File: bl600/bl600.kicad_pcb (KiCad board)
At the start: 2 copper layers, 50 x 50 mm, 27 parts, among them IC1 BL600, IC2 LK112, P1 CONN_4, P2 CONN_3X2, P4 CONN_2, P5 CONN_8, P6 CONN_8, P7 CONN_6X2, Q1 MOSFET_P, Q2 MOSFET_P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

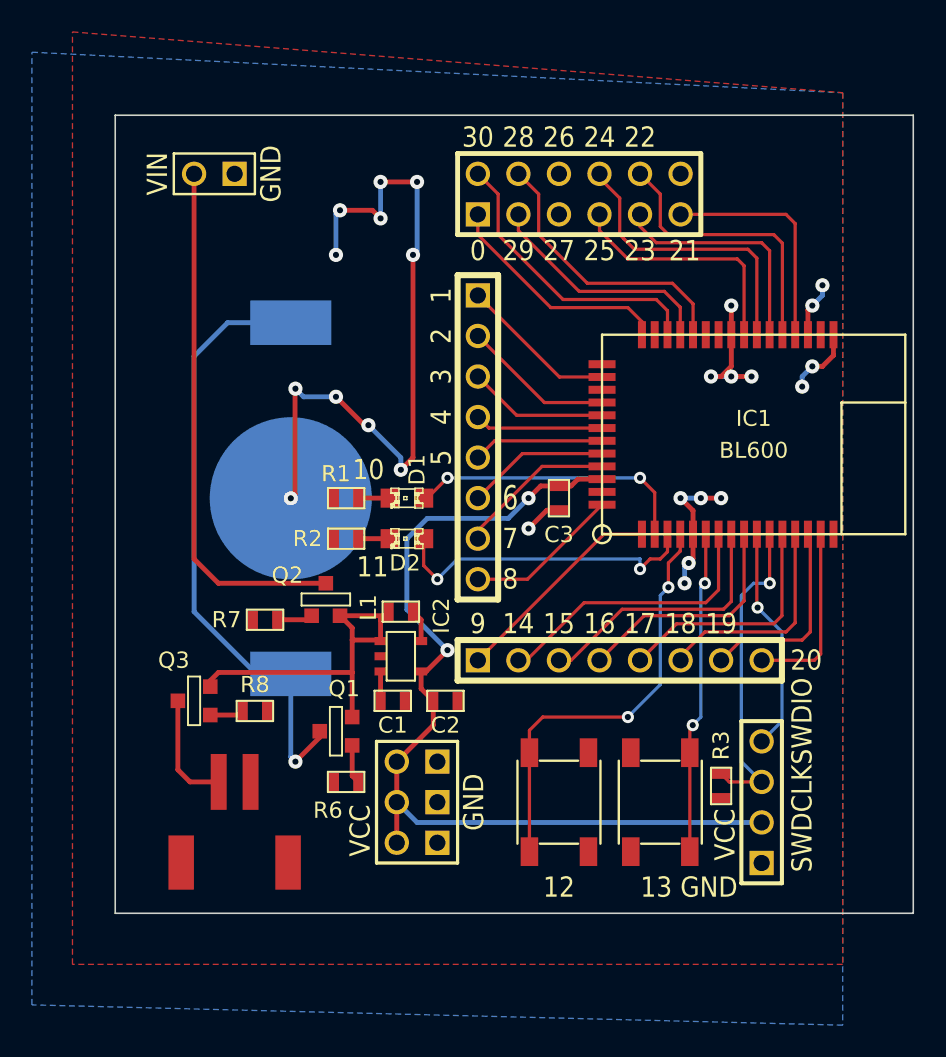
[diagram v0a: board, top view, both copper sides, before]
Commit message: BL600 add ARM 10/9 pin SWD header
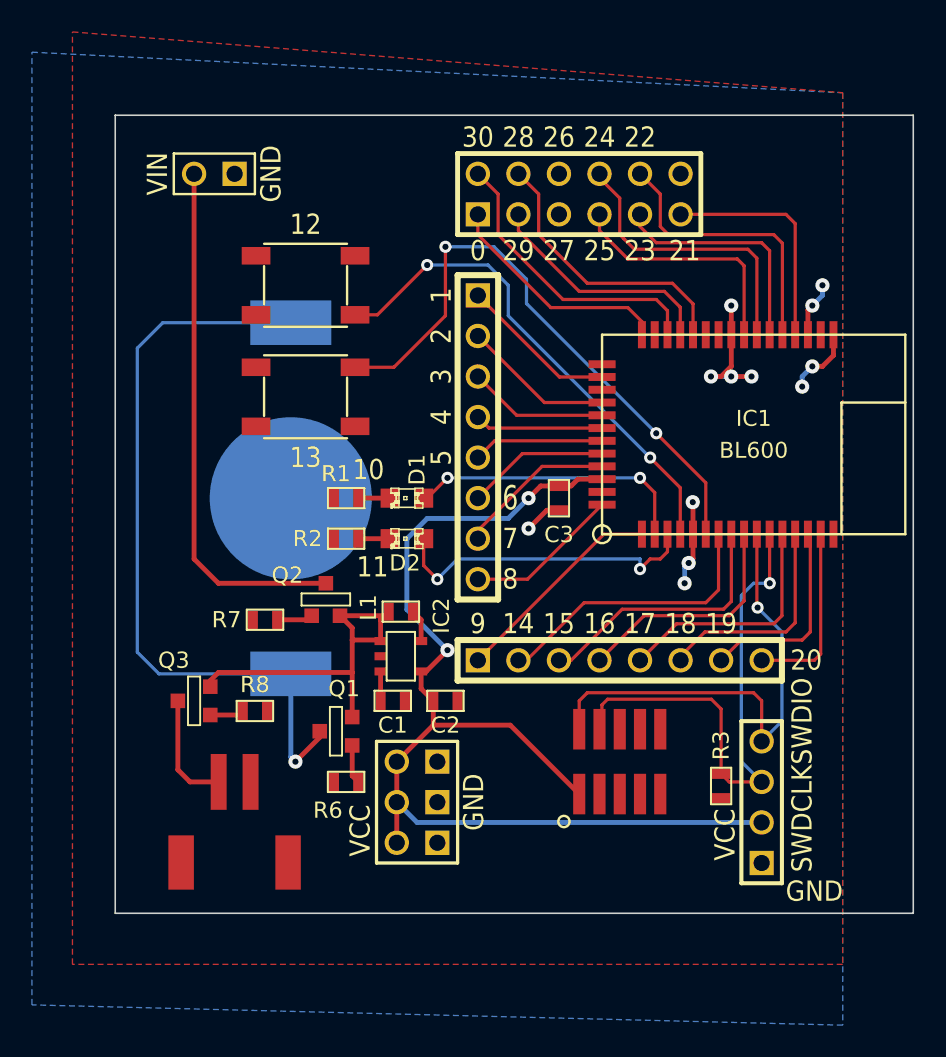
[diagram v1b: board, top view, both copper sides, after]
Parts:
- added P3: CONN_5X2, PIN_FTSH-105, F.Cu at (181.6, 190.5)
- moved SW1 36.1 mm to (161.9, 160.7), turned to 180 degrees
- moved SW2 33.8 mm to (161.9, 167.6), turned to 0 degrees
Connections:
- net /SWCLK renamed /SWDCLK
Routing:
- net GND: track 71.7 -> 23.5 mm, vias 25 -> 12
- net /BTN2: track 20.3 -> 37.9 mm
- net /SWDIO: track 14.2 -> 30.3 mm
- net /SWDCLK: track 20.1 -> 33.6 mm
- net VCC: track 59.4 -> 70.3 mm
- net N-0000017: track 38.8 -> 47.7 mm
- net /BTN1: track 26.9 -> 31.5 mm

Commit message: Connect CR2032 holder directly to 3V3
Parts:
- removed R6, R7, R8: 10K, SM0603
- moved L1 6.67 mm to (171.0, 187.0)
- moved C2 3.33 mm to (174.0, 187.0)
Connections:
- IC2 pad 4: VCC -> /3VIN
- IC2 pad 5: N-0000013 (its old number) -> /VIN
- L1 pad 1: /VIN -> /3VIN
- L1 pad 2: N-0000013 (its old number) -> VCC
- Q1 pad G: N-0000016 -> GND
- Q1 pad S: /VIN -> /3VIN
- Q2 pad G: N-0000018 (its old number) -> GND
- Q3 pad G: N-0000012 (its old number) -> GND
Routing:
- net /3VIN: track 0.00 -> 8.44 mm
- net /VIN: track 23.2 -> 15.7 mm
- net /BTN2: track 37.9 -> 44.1 mm
- net /BTN1: track 31.5 -> 37.7 mm
- net VCC: track 70.3 -> 67.3 mm, vias 2 -> 0
- net N-0000016: track 2.44 -> 0.00 mm
- net N-0000018 (its old number): track 2.26 -> 0.00 mm
- net N-0000012 (its old number): track 2.14 -> 0.00 mm
- net N-0000013 (its old number): track 2.05 -> 0.00 mm
